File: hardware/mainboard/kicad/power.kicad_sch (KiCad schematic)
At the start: 44 parts, among them J1 1S LiPo + NTC, Q2 AO3401A, SW1 HARD POWER, U2 TPS2121, U3 BQ25185DLHR, U4 TPS63802DLAR

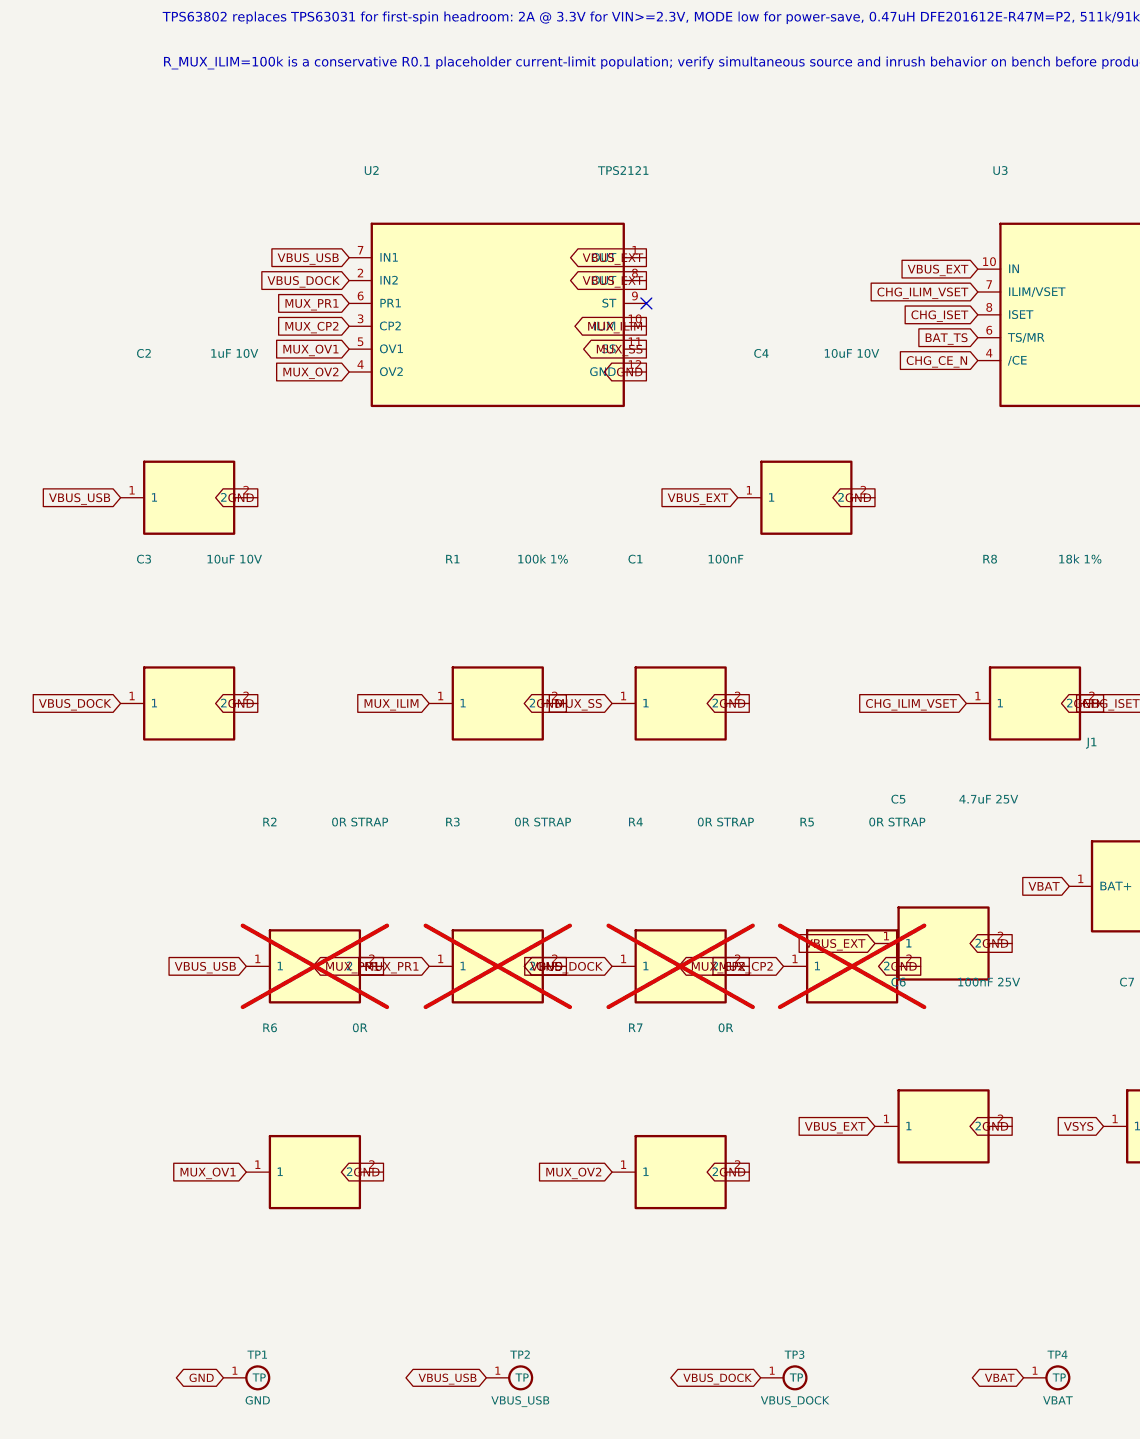
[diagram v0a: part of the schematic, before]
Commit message: hardware: preserve recovered R119 layout and verified R118 source [skip ci]
Persist the KiCad 10.0.7 project before the next routing pass. The recovered layout has 67 opens, ERC 0, parity 0 and zero RF keepout violations; routing is incomplete and fabrication is blocked. Preserve all pad and surviving copper net identities and retain an immutable R118 source archive.
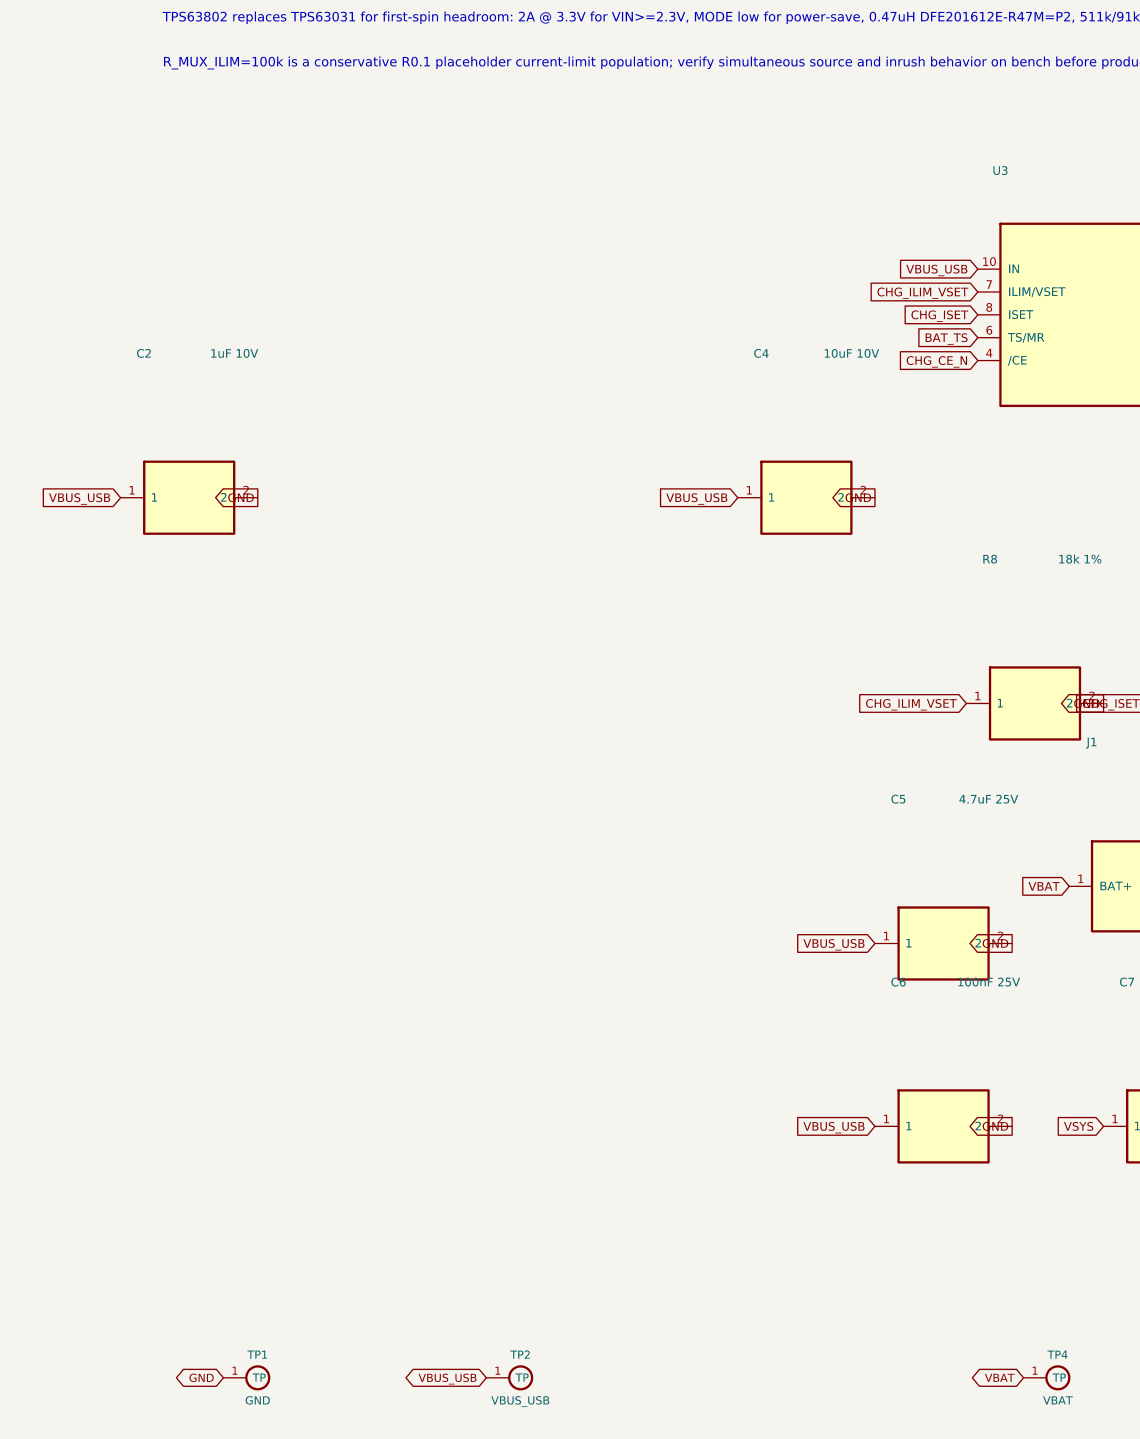
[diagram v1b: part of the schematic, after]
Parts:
- removed C1: 100nF, Capacitor_SMD:C_0603_1608Metric, symbol ENKU:C
- removed C3: 10uF 10V, Capacitor_SMD:C_0805_2012Metric, symbol ENKU:C
- removed R1: 100k 1%, Resistor_SMD:R_0603_1608Metric, symbol ENKU:R
- removed R2, R3, R4, R5: 0R STRAP, Resistor_SMD:R_0603_1608Metric, symbol ENKU:R
- removed R6, R7: 0R, Resistor_SMD:R_0603_1608Metric, symbol ENKU:R
- removed TP3: VBUS_DOCK, TestPoint:TestPoint_Pad_D1.5mm, symbol ENKU:TESTPOINT
- removed U2: TPS2121, ENKU:TPS2121_RUX0012A, symbol ENKU:TPS2121_RUX
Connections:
- net VBUS_EXT is gone; now on net VBUS_USB: C4.1, C5.1, C6.1, U3.10 (IN)
- no-connect marks 1 -> 0

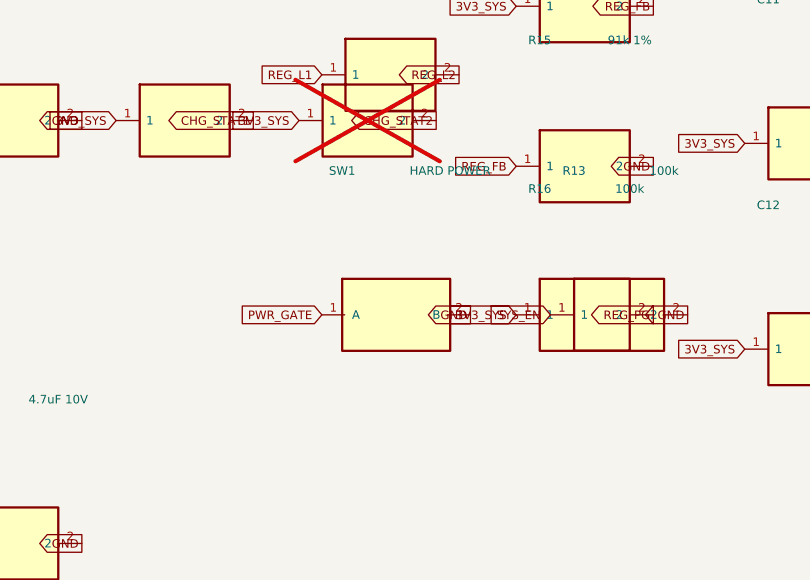
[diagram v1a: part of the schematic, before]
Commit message: R124: restore approved SW1, correct common pin and route upper-edge switch
Replace the two-pad placeholder with the approved MK-12C03-G015 three-terminal symbol and reviewed physical footprint. Preserve R29 ground and the U1 RF keepout. Native local: zero opens/ERC/parity, 109 library mismatches and 20 active hole findings. Add physical/netlist SW1 regression guard and retain A0/X1 land-pattern and mechanical-datum HOLD; NO FAB.
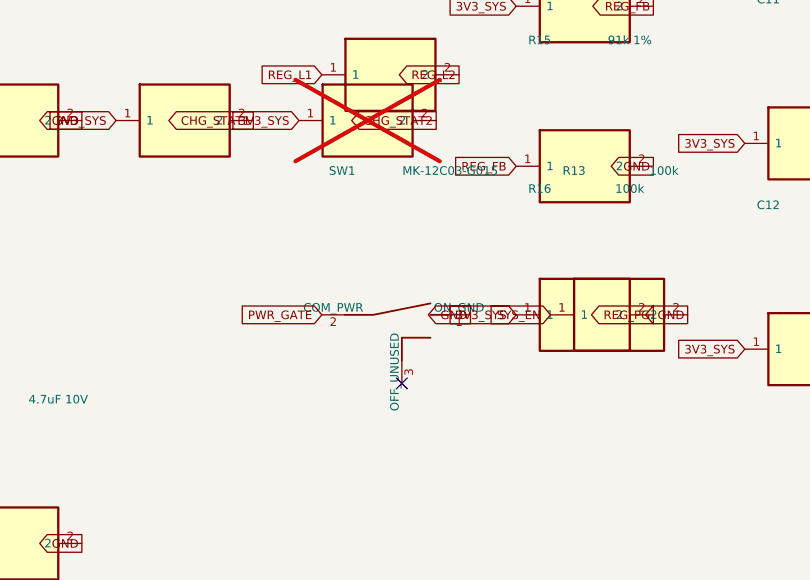
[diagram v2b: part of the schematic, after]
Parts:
- SW1: value HARD POWER -> MK-12C03-G015; footprint ENKU:HARD_POWER_SWITCH_PLACEMENT -> ENKU:GSWITCH_MK12C03_G015_DRAWING_REVIEW; symbol ENKU:SW_SPST -> ENKU:MK12C03_G015
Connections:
- net GND: now also SW1.1 (ON_GND); no longer SW1.2 (B)
- net PWR_GATE: now also SW1.2 (COM_PWR); no longer SW1.1 (A)
- no-connect marks 0 -> 1
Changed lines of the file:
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@@
 	(global_label "VBAT" (shape input) (at 154.94 152.4 0) (effects (font (size 0.95 0.95)) (justify right bottom)))
 	(global_label "GND" (shape output) (at 170.18 152.4 180) (effects (font (size 0.95 0.95)) (justify right bottom)))
-	(symbol (lib_id "ENKU:SW_SPST") (at 205.105 127 0) (unit 1) (exclude_from_sim no) (in_bom yes) (on_board yes) (dnp no)
+	(symbol (lib_id "ENKU:MK12C03_G015") (at 205.105 127 0) (unit 1) (exclude_from_sim no) (in_bom yes) (on_board yes) (dnp no)
 		(property "Reference" "SW1" (at 199.105 111 0) (effects (font (size 0.95 0.95))))
-		(property "Value" "HARD POWER" (at 211.105 111 0) (effects (font (size 0.95 0.95))))
-		(property "Footprint" "ENKU:HARD_POWER_SWITCH_PLACEMENT" (at 205.105 127 0) (effects (font (size 0.95 0.95)) (hide yes)))
-		(property "Datasheet" "~" (at 205.105 127 0) (effects (font (size 0.95 0.95)) (hide yes)))
-		(property "Description" "HARD POWER" (at 205.105 127 0) (effects (font (size 0.95 0.95)) (hide yes)))
-		(pin "1")
-		(pin "2")
+		(property "Value" "MK-12C03-G015" (at 211.105 111 0) (effects (font (size 0.95 0.95))))
+		(property "Footprint" "ENKU:GSWITCH_MK12C03_G015_DRAWING_REVIEW" (at 205.105 127 0) (effects (font (size 0.95 0.95)) (hide yes)))
+		(property "Datasheet" "https://cdn.semikey.com/upload/pdfs/a6/85/a685b04beffe80627230619bb0c8ae8e.pdf" (at 205.105 127 0) (effects (font (size 0.95 0.95)) (hide yes)))
+		(property "Description" "MK-12C03-G015" (at 205.105 127 0) (effects (font (size 0.95 0.95)) (hide yes)))
+		(pin "2")
+		(pin "1")
+		(pin "3")
 		(instances (project "enku-mainboard-r0.1" (path "/10000000-0000-4000-8000-000000000001/70000000-0000-4000-8000-000000000179" (reference "SW1") (unit 1))))
 	)
@@
 	(global_label "VSYS" (shape input) (at 312.42 143.51 0) (effects (font (size 0.95 0.95)) (justify right bottom)))
 	(global_label "PWR_GATE" (shape output) (at 327.66 143.51 180) (effects (font (size 0.95 0.95)) (justify right bottom)))
-)
+(no_connect (at 205.74 134.62))
+)

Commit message: R125: correct manufacturer Q1/Q2/U9 lands and guard full copper, netlist and assembly layers
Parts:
- Q2: footprint Package_TO_SOT_SMD:SOT-23 -> ENKU:AO3401A_AOS_SOT23
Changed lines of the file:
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@@
  (property "Reference" "Q2" (at 286.465 127.50999999999999 0) (effects (font (size 0.95 0.95))))
  (property "Value" "AO3401A" (at 296.465 127.50999999999999 0) (effects (font (size 0.95 0.95))))
- (property "Footprint" "Package_TO_SOT_SMD:SOT-23" (at 291.465 143.51 0) (effects (font (size 0.95 0.95)) (hide yes)))
+ (property "Footprint" "ENKU:AO3401A_AOS_SOT23" (at 291.465 143.51 0) (effects (font (size 0.95 0.95)) (hide yes)))
  (property "Datasheet" "https://www.aosmd.com/sites/default/files/res/data_sheets/AO3401A.pdf" (at 291.465 143.51 0) (effects (font (size 0.95 0.95)) (hide yes)))
  (property "Description" "AO3401A" (at 291.465 143.51 0) (effects (font (size 0.95 0.95)) (hide yes)))

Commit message: R126: select 61 exact components, correct physical lands and local routing, preserve full source; NO FAB
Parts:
- C10, C6: footprint Capacitor_SMD:C_0603_1608Metric -> ENKU:C_CC0603_YAGEO_REFLOW_TRANSFER; Assembly (none) -> FIT; MPN (none) -> CC0603KRX7R9BB104; Manufacturer (none) -> Yageo; Voltage (none) -> 50V
- C11, C12: footprint Capacitor_SMD:C_0805_2012Metric -> ENKU:C_CC0805_YAGEO_REFLOW_TRANSFER; Assembly (none) -> FIT; MPN (none) -> CC0805MKX5R6BB226; Manufacturer (none) -> Yageo; Voltage (none) -> 10V
- C2: footprint Capacitor_SMD:C_0805_2012Metric -> ENKU:C_CC0805_YAGEO_REFLOW_TRANSFER; Assembly (none) -> FIT; MPN (none) -> CC0805KKX7R6BB105; Manufacturer (none) -> Yageo; Voltage (none) -> 10V
- C4, C9: footprint Capacitor_SMD:C_0805_2012Metric -> ENKU:C_CC0805_YAGEO_REFLOW_TRANSFER; Assembly (none) -> FIT; MPN (none) -> CC0805KKX5R6BB106; Manufacturer (none) -> Yageo; Voltage (none) -> 10V
- C5: footprint Capacitor_SMD:C_0805_2012Metric -> ENKU:C_CC0805_YAGEO_REFLOW_TRANSFER; Assembly (none) -> FIT; MPN (none) -> CC0805KKX7R8BB475; Manufacturer (none) -> Yageo; Voltage (none) -> 25V
- C7: footprint Capacitor_SMD:C_0805_2012Metric -> ENKU:C_CC0805_YAGEO_REFLOW_TRANSFER; Assembly (none) -> FIT; MPN (none) -> CC0805KKX5R8BB106; Manufacturer (none) -> Yageo; Voltage (none) -> 25V
- C8: footprint Capacitor_SMD:C_0805_2012Metric -> ENKU:C_CC0805_YAGEO_REFLOW_TRANSFER; Assembly (none) -> FIT; MPN (none) -> CC0805KKX5R6BB475; Manufacturer (none) -> Yageo; Voltage (none) -> 10V
- R10, R13, R16, R40: footprint Resistor_SMD:R_0603_1608Metric -> ENKU:R_RC0603_YAGEO_REFLOW; Assembly (none) -> FIT; MPN (none) -> RC0603FR-07100KL; Manufacturer (none) -> Yageo
- R11: footprint Resistor_SMD:R_0603_1608Metric -> ENKU:R_RC0603_YAGEO_REFLOW; Assembly (none) -> FIT; MPN (none) -> RC0603FR-0710KL; Manufacturer (none) -> Yageo
- R12: footprint Resistor_SMD:R_0603_1608Metric -> ENKU:R_RC0603_YAGEO_REFLOW; Assembly (none) -> DNP; MPN (none) -> RC0603FR-0710KL; Manufacturer (none) -> Yageo
- R14: footprint Resistor_SMD:R_0603_1608Metric -> ENKU:R_RC0603_YAGEO_REFLOW; Assembly (none) -> FIT; MPN (none) -> RC0603FR-07511KL; Manufacturer (none) -> Yageo
- R15: footprint Resistor_SMD:R_0603_1608Metric -> ENKU:R_RC0603_YAGEO_REFLOW; Assembly (none) -> FIT; MPN (none) -> RC0603FR-0791KL; Manufacturer (none) -> Yageo
- R8: footprint Resistor_SMD:R_0603_1608Metric -> ENKU:R_RC0603_YAGEO_REFLOW; Assembly (none) -> FIT; MPN (none) -> RC0603FR-0718KL; Manufacturer (none) -> Yageo
- R9: footprint Resistor_SMD:R_0603_1608Metric -> ENKU:R_RC0603_YAGEO_REFLOW; Assembly (none) -> FIT; MPN (none) -> RC0603FR-071KL; Manufacturer (none) -> Yageo

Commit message: R127: finish passive MPN selection and correct USB VBUS capacitance
Select exact parts and nominal lands for the remaining 15 capacitors and R70/R71/R37. Reduce C4 from10uF/10V to1uF/25V, taking direct VBUS capacitance from15.8 to6.8uF. Preserve all417 original pad and2639 Cu identities/nets, with only3 declared EPD_VCI vertex adjustments.

Native KiCad10.0.7: opens0/ERC0/parity0/DRC47(27library+20holes). Add independent79-part, source and native-netlist numeric power guards. Record unqualified Ceff, inrush, EPD pulse/process gates; NO FAB.
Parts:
- C4: value 10uF 10V -> 1uF 25V; MPN CC0805KKX5R6BB106 -> CC0805KKX7R8BB105; Voltage 10V -> 25V
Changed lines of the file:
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@@
 	(symbol (lib_id "ENKU:C") (at 96.52 82.55 0) (unit 1) (exclude_from_sim no) (in_bom yes) (on_board yes) (dnp no)
 		(property "Reference" "C4" (at 91.52 66.55 0) (effects (font (size 0.95 0.95))))
-		(property "Value" "10uF 10V" (at 101.52 66.55 0) (effects (font (size 0.95 0.95))))
+		(property "Value" "1uF 25V" (at 101.52 66.55 0) (effects (font (size 0.95 0.95))))
 		(property "Footprint" "ENKU:C_CC0805_YAGEO_REFLOW_TRANSFER" (at 96.52 82.55 0) (effects (font (size 0.95 0.95)) (hide yes)))
-		(property "Datasheet" "https://yageogroup.com/download/specsheet/CC0805KKX5R6BB106" (at 96.52 82.55 0) (effects (font (size 0.95 0.95)) (hide yes)))
-		(property "Description" "10uF 10V" (at 96.52 82.55 0) (effects (font (size 0.95 0.95)) (hide yes)))
+		(property "Datasheet" "https://yageogroup.com/download/specsheet/CC0805KKX7R8BB105" (at 96.52 82.55 0) (effects (font (size 0.95 0.95)) (hide yes)))
+		(property "Description" "USB VBUS bypass; R127 reduces direct VBUS capacitor budget from15.8 to6.8uF. BQ25185 IN effective capacitance and actual inrush require qualification." (at 96.52 82.55 0) (effects (font (size 0.95 0.95)) (hide yes)))
 		(pin "1")
 		(pin "2")
 		(instances (project "enku-mainboard-r0.1" (path "/10000000-0000-4000-8000-000000000001/70000000-0000-4000-8000-000000000099" (reference "C4") (unit 1))))
-		(property "MPN" "CC0805KKX5R6BB106" (at 0 0 0) (effects (font (size .8 .8)) (hide yes)))
+		(property "MPN" "CC0805KKX7R8BB105" (at 0 0 0) (effects (font (size .8 .8)) (hide yes)))
 		(property "Manufacturer" "Yageo" (at 0 0 0) (effects (font (size .8 .8)) (hide yes)))
 		(property "Assembly" "FIT" (at 0 0 0) (effects (font (size .8 .8)) (hide yes)))
-		(property "Voltage" "10V" (at 0 0 0) (effects (font (size .8 .8)) (hide yes)))
+		(property "Voltage" "25V" (at 0 0 0) (effects (font (size .8 .8)) (hide yes)))
 	)
 	(global_label "VBUS_USB" (shape input) (at 88.9 82.55 0) (effects (font (size 0.95 0.95)) (justify right bottom)))

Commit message: R129: fix IC stencil apertures, pin-1 marking and native assembly classification
Verify six active IC pin maps and 97 native CPL placements. Preserve all 425 original pads, nets and 2639 tracks/vias; retain the 20 active intrinsic hole-clearance findings as fabrication gates. Add independent native KiCad checks and exact source-preservation guards.
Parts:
- TP1: footprint TestPoint:TestPoint_Pad_D1.5mm -> ENKU:SERVICE_PAD_D1_5_NO_PASTE; Assembly (none) -> BARE_PCB; Probe Label (none) -> GND; now left out of the parts list
- TP2: footprint TestPoint:TestPoint_Pad_D1.5mm -> ENKU:SERVICE_PAD_D1_5_NO_PASTE; Assembly (none) -> BARE_PCB; Probe Label (none) -> USB5; now left out of the parts list
- TP4: footprint TestPoint:TestPoint_Pad_D1.5mm -> ENKU:SERVICE_PAD_D1_5_NO_PASTE; Assembly (none) -> BARE_PCB; Probe Label (none) -> VBAT; now left out of the parts list
- TP5: footprint TestPoint:TestPoint_Pad_D1.5mm -> ENKU:SERVICE_PAD_D1_5_NO_PASTE; Assembly (none) -> BARE_PCB; Probe Label (none) -> VSYS; now left out of the parts list
- TP6: footprint TestPoint:TestPoint_Pad_D1.5mm -> ENKU:SERVICE_PAD_D1_5_NO_PASTE; Assembly (none) -> BARE_PCB; Probe Label (none) -> 3V3; now left out of the parts list
- TP7: footprint TestPoint:TestPoint_Pad_D1.5mm -> ENKU:SERVICE_PAD_D1_5_NO_PASTE; Assembly (none) -> BARE_PCB; Probe Label (none) -> EN; now left out of the parts list
- TP8: footprint TestPoint:TestPoint_Pad_D1.5mm -> ENKU:SERVICE_PAD_D1_5_NO_PASTE; Assembly (none) -> BARE_PCB; Probe Label (none) -> PG; now left out of the parts list
- U3: footprint ENKU:BQ25185_DLH0010A -> ENKU:BQ25185_DLH0010A_TI_STENCIL; Assembly (none) -> FIT; Charge Profile (none) -> 4.2V/500mA input/300mA fast charge;RevB timer360min;battery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; MPN (none) -> BQ25185DLHR; Manufacturer (none) -> Texas Instruments
- U4: footprint ENKU:TPS63802_DLA0010A -> ENKU:TPS63802_DLA0010A_SPLIT_PASTE; Assembly (none) -> FIT; MPN (none) -> TPS63802DLAR; Manufacturer (none) -> Texas Instruments
